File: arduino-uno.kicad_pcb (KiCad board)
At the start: 2 copper layers, 68.6 x 53.3 mm, 52 parts, among them J1 Jack-DC, J2 USB_B, J3 Conn_02x03_Odd_Even, J4 Conn_02x02_Odd_Even, J5 Conn_02x03_Odd_Even, P1 Power, P2 Analog, P3 Digital, P4 Digital, P5 CONN_01X01, P6 CONN_01X01, P7 CONN_01X01, P8 CONN_01X01, Q1 FDN340P, SW1 SW_Push, U1 NCP1117-5.0_SOT223, U2 LMV358IDGKR, U3 LP2985-3.3, U4 ATmega16U2-MU, U5 ATmega328P-PU, Y1 Crystal, Y2 CSTCE16M0V53-R0

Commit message: place finish
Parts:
- C10: value C -> 100n
- JP1: moved to B.Cu
- JP2: footprint Jumper:SolderJumper-2_P1.3mm_Bridged_Pad1.0x1.5mm -> Jumper:SolderJumper-2_P1.3mm_Open_Pad1.0x1.5mm
- moved C3 82.7 mm to (136.4, 110.4), turned to 90 degrees
- moved C5 78.7 mm to (154.2, 116.5)
- moved C4 74.4 mm to (128.0, 110.4), turned to 90 degrees
- moved C9 72.9 mm to (138.5, 82.2)
- moved JP1 62.5 mm to (120.3, 84.5)
- moved R1 59.8 mm to (129.5, 97.4)
- moved C8 57.0 mm to (122.9, 97.4), turned to 180 degrees
- moved C7 56.7 mm to (138.5, 96.7)
- moved C6 54.5 mm to (122.9, 95.3), turned to 180 degrees
- moved C10 44.2 mm to (138.5, 94.7), turned to 180 degrees
- moved RN2 42.3 mm to (138.5, 102.8)
- moved C11 30.1 mm to (122.9, 85.0)
- moved U3 0.70 mm to (132.2, 110.4)
- moved JP2 0.56 mm to (138.5, 99.2)
- moved Q1 0.53 mm to (119.1, 101.0)
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
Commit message: route finish
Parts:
- SW1: footprint Button_Switch_SMD:SW_SPST_B3S-1000 -> Button_Switch_SMD:SW_SPST_PTS645
- turned RN3 to 180 degrees
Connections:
- RN3 pad 5: Net-(J2-Pad2) -> Net-(J2-Pad3)
- RN3 pad 8: Net-(J2-Pad3) -> Net-(J2-Pad2)
- U4 pad 29: Net-(RN3-Pad1) -> Net-(RN3-Pad4)
- U4 pad 30: Net-(RN3-Pad4) -> Net-(RN3-Pad1)
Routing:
- net GND: track 0.00 -> 317.2 mm, vias 0 -> 4
- net +5V: track 0.00 -> 186.7 mm, vias 0 -> 5
- net /Main/Reset: track 0.00 -> 136.6 mm, vias 0 -> 2
- net /Main/13(SCK): track 0.00 -> 94.8 mm, vias 0 -> 1
- net /Main/VIN: track 0.00 -> 93.0 mm, vias 0 -> 1
- net /Main/A5(SCL): track 0.00 -> 90.3 mm
- net /Main/A4(SDA): track 0.00 -> 88.4 mm
- net /Main/11(**/MOSI): track 0.00 -> 85.7 mm
- net /Main/0(Rx): track 0.00 -> 84.3 mm, vias 0 -> 1
- net /Main/12(MISO): track 0.00 -> 84.1 mm
- net /Main/1(Tx): track 0.00 -> 80.7 mm, vias 0 -> 1
- net Net-(D3-Pad2): track 0.00 -> 67.1 mm
- net /Main/AREF: track 0.00 -> 60.8 mm
- net /Main/9(**): track 0.00 -> 48.4 mm
- net Net-(RN1-Pad1): track 0.00 -> 45.4 mm
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
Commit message: update
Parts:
- moved RN2 0.40 mm to (138.5, 102.4)
- moved FB1 0.30 mm to (118.3, 81.0)
- moved SW1 0.30 mm to (117.3, 76.5)
- moved J2 0.10 mm to (118.2, 89.6)
- moved D3 0.10 mm to (123.6, 80.6)
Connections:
- U2 pad 4: (no net) -> GND
- U2 pad 8: (no net) -> +5V
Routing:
- net GND: track 317.2 -> 288.4 mm
- net /Main/0(Rx): track 84.3 -> 69.7 mm
- net /Main/10(**/SS): track 42.1 -> 49.3 mm
- net /Main/12(MISO): track 84.1 -> 91.3 mm
- net /Main/11(**/MOSI): track 85.7 -> 89.5 mm
- net Net-(F1-Pad2): track 14.7 -> 11.1 mm
- net /Main/Reset: track 136.6 -> 139.9 mm, vias 2 -> 3
- net Net-(C7-Pad1): track 18.6 -> 16.0 mm
- net /Power/USBVCC: track 21.0 -> 23.0 mm
- net /Main/9(**): track 48.4 -> 50.3 mm
- net /Main/AREF: track 60.8 -> 62.6 mm
- net /Main/DTR: track 17.5 -> 19.1 mm
- net Net-(D4-Pad1): track 8.21 -> 9.70 mm
- net /Main/13(SCK): track 94.8 -> 96.0 mm
- net +5V: track 186.7 -> 185.7 mm, vias 5 -> 4
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- added copper zone on F.Cu, net GND
- added copper zone on B.Cu, net Net-(FB1-Pad2)

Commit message: route finish
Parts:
- RESET: renamed from SW1; value SW_Push -> RESET
- moved FB1 16.7 mm to (118.4, 97.7)
- moved C6 2.14 mm to (123.4, 97.4)
- moved C8 2.05 mm to (123.4, 95.4)
- moved C5 1.27 mm to (154.2, 115.2)
- moved U4 1.27 mm to (131.3, 93.1)
- moved P6 1.18 mm to (177.0, 119.9)
- moved J3 1.02 mm to (132.3, 79.4)
- moved J4 1.02 mm to (132.3, 84.5)
- moved D3 0.61 mm to (124.2, 80.6)
- moved C11 0.51 mm to (123.4, 85.0)
- moved RN3 0.51 mm to (123.4, 90.1)
- moved RV1 0.51 mm to (123.4, 87.0)
- moved RV2 0.51 mm to (123.4, 93.3)
- moved D6 0.25 mm to (170.4, 99.1)
- moved R1 0.25 mm to (129.8, 97.4)
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- renumbered JP1 to GROUND, J5 to ICSP, D7 to L, D2 to ON, JP2 to RESET-EN, D5 to RX, D4 to TX
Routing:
- net +5V: track 185.7 -> 249.8 mm
- net Net-(D3-Pad2): track 68.1 -> 90.6 mm, vias 0 -> 1
- net /Main/A5(SCL): track 91.0 -> 101.0 mm
- net /Main/9(**): track 50.3 -> 42.1 mm
- net /USB/MOSI2: track 13.2 -> 20.9 mm
- net /Main/12(MISO): track 91.3 -> 84.5 mm
- net /Main/1(Tx): track 81.1 -> 74.8 mm, vias 1 -> 0
- net /Main/0(Rx): track 69.7 -> 74.9 mm, vias 1 -> 0
- net Net-(F1-Pad2): track 11.1 -> 16.3 mm
- net Net-(FB1-Pad2): track 33.3 -> 28.3 mm, vias 0 -> 1
- net GND: track 288.4 -> 292.9 mm, vias 4 -> 3
- net /Main/Reset: track 139.9 -> 144.0 mm, vias 3 -> 2
- net Net-(C6-Pad1): track 14.4 -> 10.6 mm
- net /Main/10(**/SS): track 49.3 -> 46.1 mm
- net Net-(D4-Pad1): track 9.70 -> 7.08 mm
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- added copper zone on B.Cu, net Net-(FB1-Pad1)
- removed copper zone on B.Cu, net Net-(FB1-Pad2)
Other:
- board text added: "12"
- board text added: "13"
- board text added: "2"
- board text added: "3V3"
- board text added: "4"
- board text added: "5V"
- board text added: "7"
- board text added: "8"
- board text added: "A0"
- board text added: "A1"
- board text added: "A2"
- board text added: "A3"
- board text added: "A4"
- board text added: "A5"
- board text added: "ANALOG IN"
- board text added: "AREF"
- board text added: "DIGITAL"
- board text added: "GND"
- board text added: "IOREF"
- board text added: "POWER"
- board text added: "RESET"
- board text added: "RX◀0"
- board text added: "TX▶1"
- board text added: "VIN"
- board text added: "[⁓=PWM]"
- board text added: "⁓10"
- board text added: "⁓11"
- board text added: "⁓3"
- board text added: "⁓5"
- board text added: "⁓6"
- board text added: "⁓9"

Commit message: add logos
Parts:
- added G***: LOGO, LOGO, B.Cu at (167.9, 81.7)
- added G***: LOGO, LOGO, F.Cu at (149.7, 92.1)
- added REF**: KiCAD Logo, Symbol:Symbol_KiCAD-Logo_CopperAndSilkScreenTop, B.Cu at (120.2, 108.4)
- added REF**: Symbol_Barrel_Polarity, Symbol:Symbol_Barrel_Polarity, F.Cu at (112.7, 109.9)
- added REF**: CE-Logo_8.5x6mm_SilkScreen, Symbol:CE-Logo_8.5x6mm_SilkScreen, B.Cu at (170.0, 118.7)
- added REF**: FCC-Logo_7.3x6mm_SilkScreen, Symbol:FCC-Logo_7.3x6mm_SilkScreen, B.Cu at (161.0, 118.7)
- added REF**: RoHS-Logo_6mm_SilkScreen, Symbol:RoHS-Logo_6mm_SilkScreen, B.Cu at (146.2, 118.7)
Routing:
- added copper zone on B.Cu, net GND
- removed copper zone on B.Cu, net Net-(FB1-Pad1)
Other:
- board text added: "+"
- board text added: "-"
- board text added: "BOARD MODEL"
- board text added: "Created by Yang Le Based on Arduino UNO Rev3 12/2018 Ver 0.5"
- board text added: "DESIGN IN ITALY"
- board text added: "DESIGNED WITH"
- board text added: "OPEN-SOURCE ELECTRONICS PROTOTYPING PLATFORM"
- board text added: "UNO"
- board text added: "WWW.ARDUINO.CC"
- board text added: "www.arduino.cc"

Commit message: update
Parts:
- added G***: LOGO, LOGO, B.Cu at (121.8, 100.3)
- moved REF** 1.59 mm to (121.8, 108.4)
- moved REF** 0.64 mm to (112.7, 109.2)

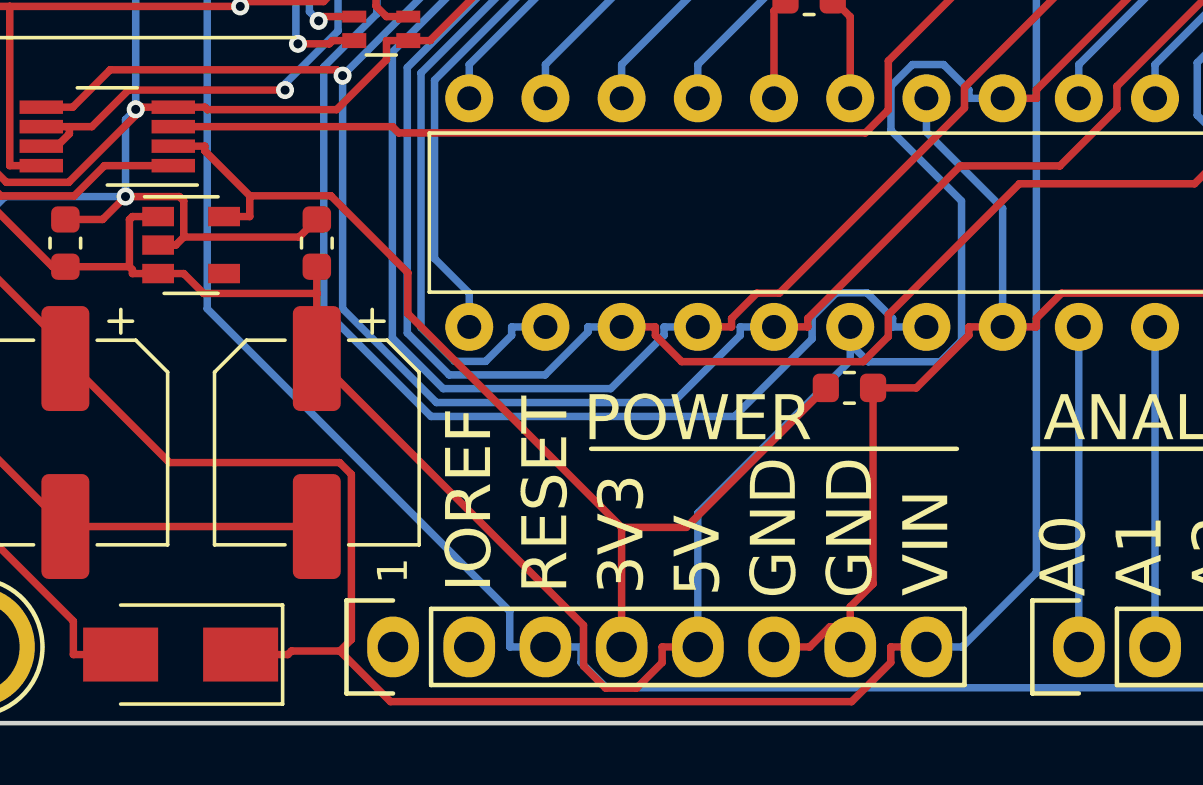
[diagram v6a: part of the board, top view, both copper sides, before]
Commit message: replace two Caps
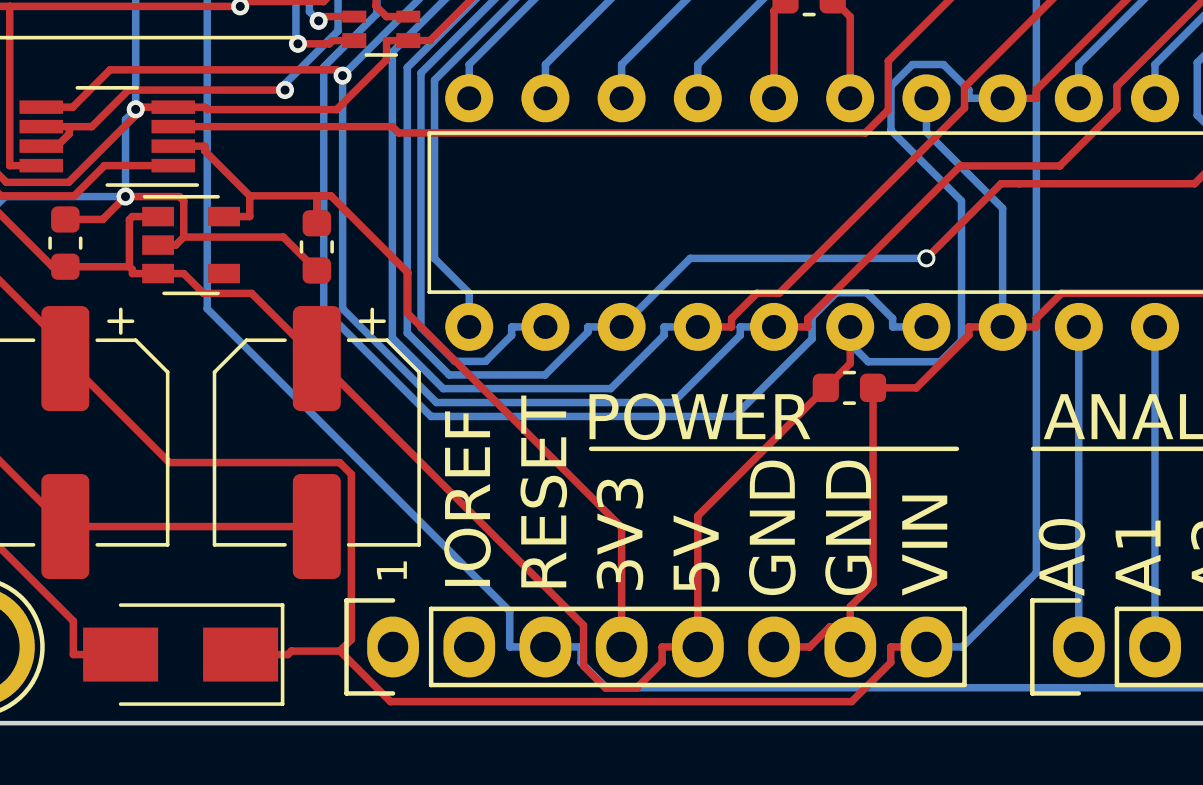
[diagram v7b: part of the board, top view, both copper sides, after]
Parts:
- moved C3 18.4 mm to (154.2, 115.2), turned to 0 degrees
- moved C5 18.4 mm to (136.4, 110.5), turned to 270 degrees
- renumbered G*** to G1, G*** to G2, G*** to G3, REF** to REF1, REF** to REF2, REF** to REF3, REF** to REF4, REF** to REF5
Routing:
- net +3V3: track 35.4 -> 27.5 mm
- net +5V: track 249.8 -> 248.2 mm
- net /Main/11(**/MOSI): track 88.2 -> 86.6 mm, vias 0 -> 1

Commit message: ready to fab
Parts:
- ICSP, J3: value Conn_02x03_Odd_Even -> Conn_02x03
- J4: value Conn_02x02_Odd_Even -> Conn_02x02
- U1: value NCP1117-5.0_SOT223 -> NCP1117-5.0
